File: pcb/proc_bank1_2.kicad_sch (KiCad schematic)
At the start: 1 part

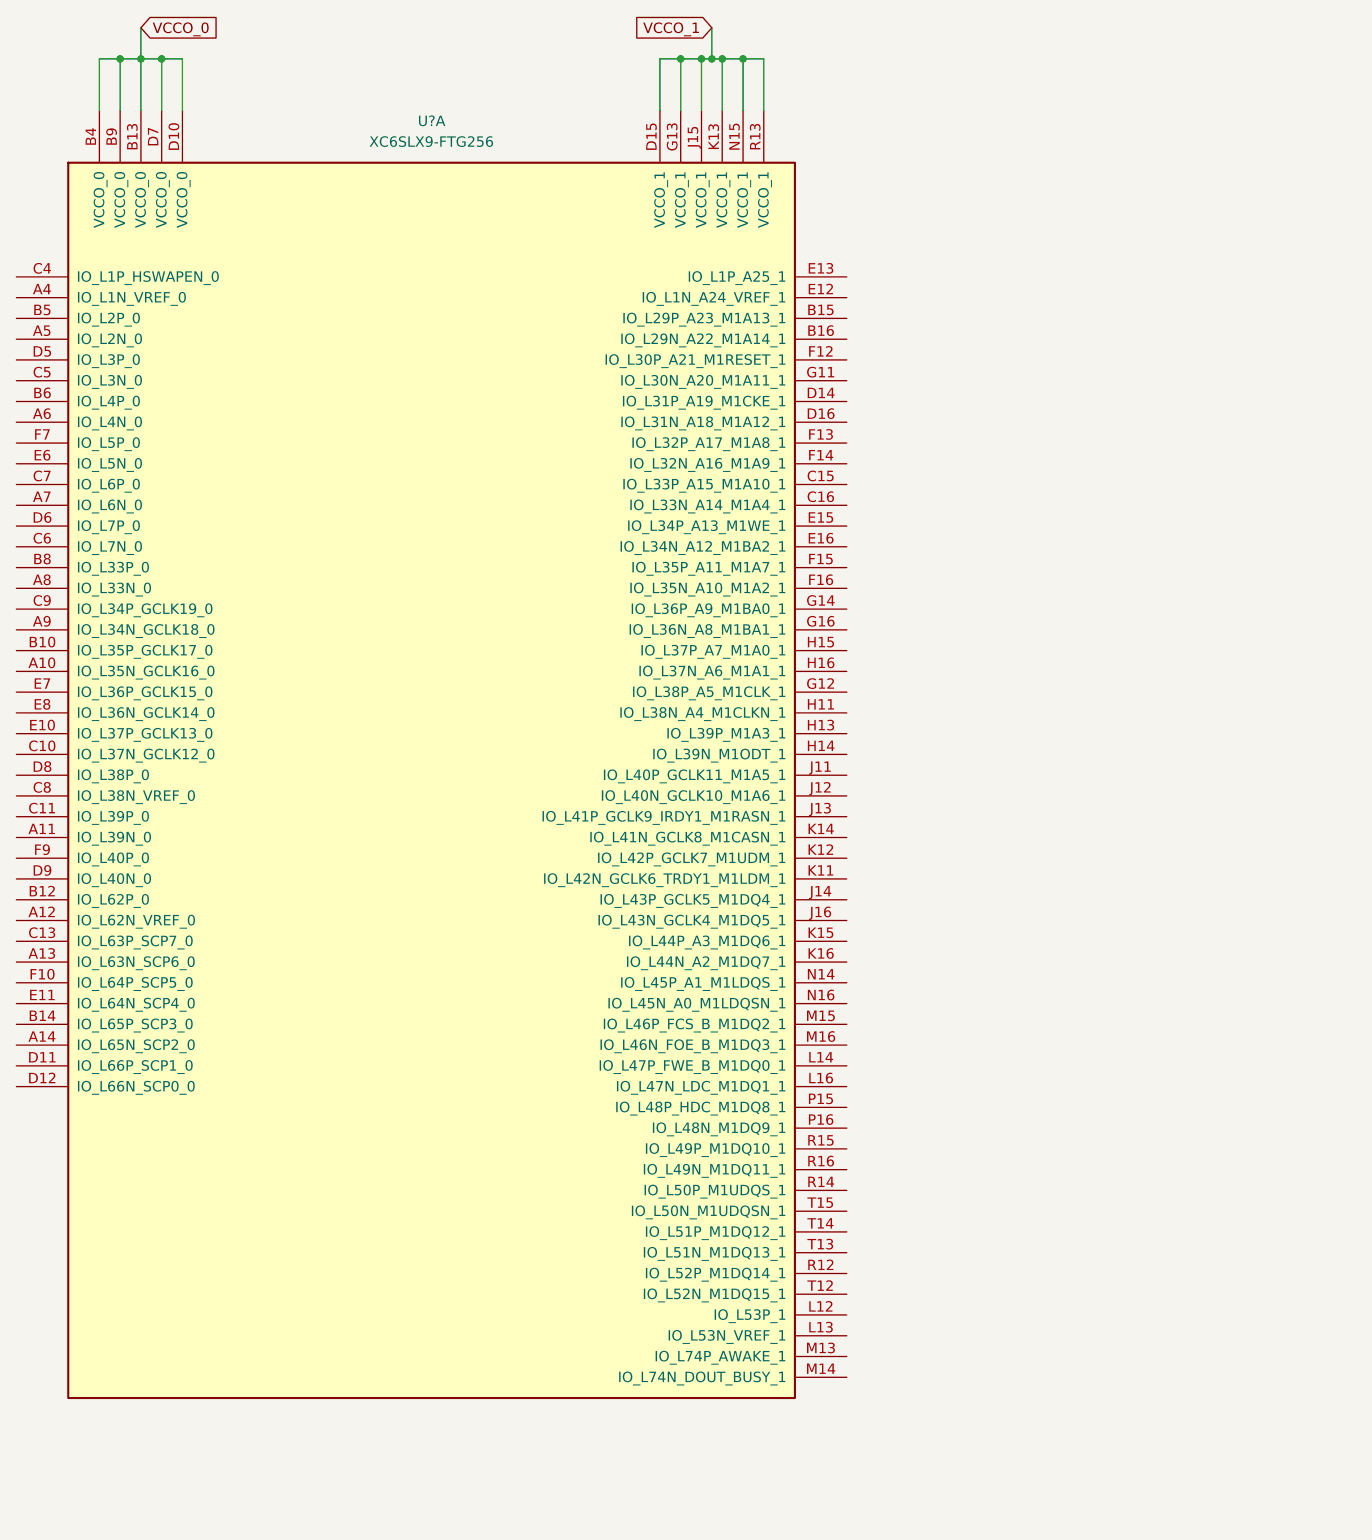
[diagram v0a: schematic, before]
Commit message: add flash memory
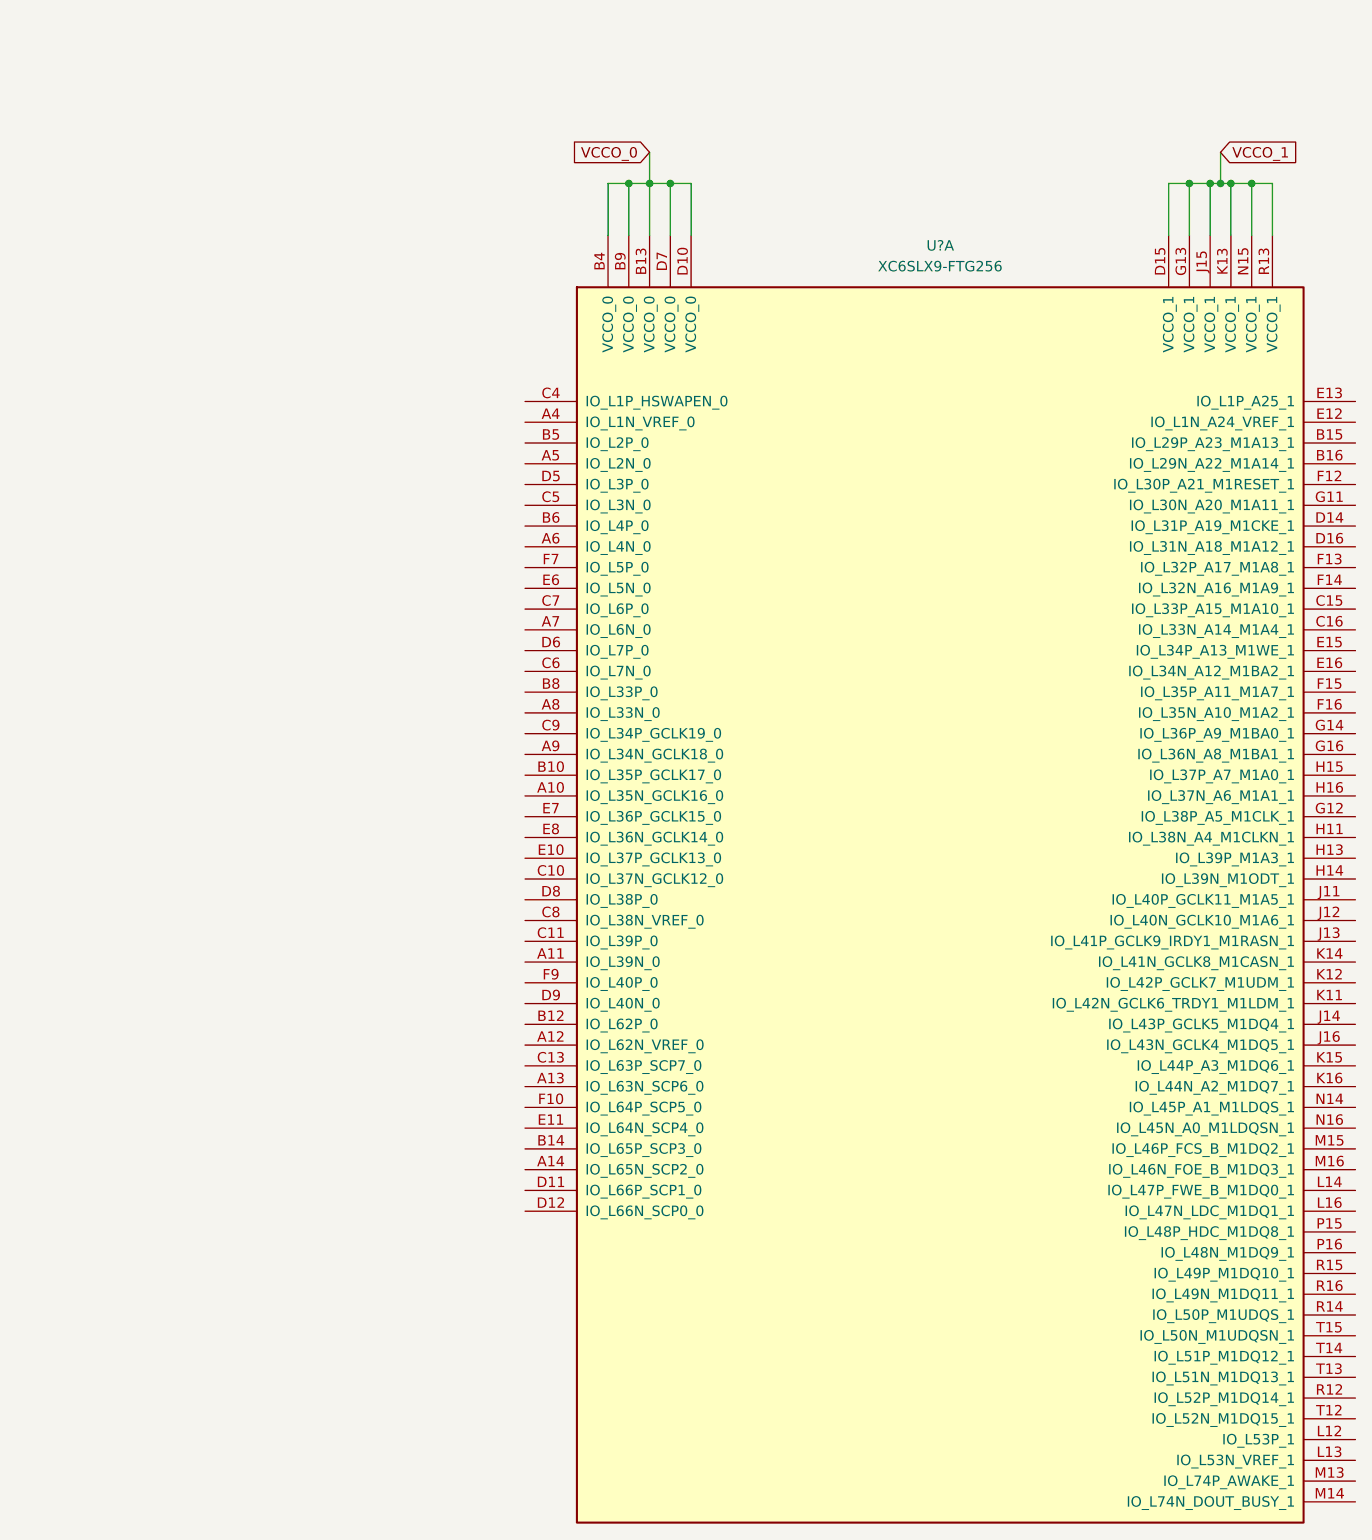
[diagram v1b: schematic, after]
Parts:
- removed U?: XC6SLX9-FTG256, symbol FPGA_Xilinx_Spartan6:XC6SLX9-FTG256
- added U?: XC6SLX9-FTG256, symbol FPGA_Xilinx_Spartan6:XC6SLX9-FTG256
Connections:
- net VCCO_0: now also U?.B13 (VCCO_0), U?.B4 (VCCO_0), U?.B9 (VCCO_0), U?.D10 (VCCO_0), U?.D7 (VCCO_0)
- net VCCO_1: now also U?.D15 (VCCO_1), U?.G13 (VCCO_1), U?.J15 (VCCO_1), U?.K13 (VCCO_1), U?.N15 (VCCO_1), U?.R13 (VCCO_1)
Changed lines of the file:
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@@
 (kicad_sch (version 20210126) (generator eeschema)
-  (paper "User" 200 240.005)
-  (junction (at 60.96 33.02) (diameter 0.9144) (color 0 0 0 0))
-  (junction (at 63.5 33.02) (diameter 0.9144) (color 0 0 0 0))
-  (junction (at 66.04 33.02) (diameter 0.9144) (color 0 0 0 0))
-  (junction (at 129.54 33.02) (diameter 0.9144) (color 0 0 0 0))
-  (junction (at 132.08 33.02) (diameter 0.9144) (color 0 0 0 0))
-  (junction (at 133.35 33.02) (diameter 0.9144) (color 0 0 0 0))
-  (junction (at 134.62 33.02) (diameter 0.9144) (color 0 0 0 0))
-  (junction (at 137.16 33.02) (diameter 0.9144) (color 0 0 0 0))
-  (wire (pts (xy 58.42 33.02) (xy 60.96 33.02))
+  (paper "User" 319.989 280.01)
+  (junction (at 123.19 48.26) (diameter 0.9144) (color 0 0 0 0))
+  (junction (at 125.73 48.26) (diameter 0.9144) (color 0 0 0 0))
+  (junction (at 128.27 48.26) (diameter 0.9144) (color 0 0 0 0))
+  (junction (at 191.77 48.26) (diameter 0.9144) (color 0 0 0 0))
+  (junction (at 194.31 48.26) (diameter 0.9144) (color 0 0 0 0))
+  (junction (at 195.58 48.26) (diameter 0.9144) (color 0 0 0 0))
+  (junction (at 196.85 48.26) (diameter 0.9144) (color 0 0 0 0))
+  (junction (at 199.39 48.26) (diameter 0.9144) (color 0 0 0 0))
+  (wire (pts (xy 120.65 48.26) (xy 123.19 48.26))
     (stroke (width 0) (type solid) (color 0 0 0 0))
   )
-  (wire (pts (xy 58.42 39.37) (xy 58.42 33.02))
+  (wire (pts (xy 120.65 54.61) (xy 120.65 48.26))
     (stroke (width 0) (type solid) (color 0 0 0 0))
   )
-  (wire (pts (xy 60.96 33.02) (xy 60.96 39.37))
+  (wire (pts (xy 123.19 48.26) (xy 123.19 54.61))
     (stroke (width 0) (type solid) (color 0 0 0 0))
   )
-  (wire (pts (xy 60.96 33.02) (xy 63.5 33.02))
+  (wire (pts (xy 123.19 48.26) (xy 125.73 48.26))
     (stroke (width 0) (type solid) (color 0 0 0 0))
   )
-  (wire (pts (xy 63.5 29.21) (xy 63.5 33.02))
+  (wire (pts (xy 125.73 44.45) (xy 125.73 48.26))
     (stroke (width 0) (type solid) (color 0 0 0 0))
   )
-  (wire (pts (xy 63.5 33.02) (xy 63.5 39.37))
+  (wire (pts (xy 125.73 48.26) (xy 125.73 54.61))
     (stroke (width 0) (type solid) (color 0 0 0 0))
   )
-  (wire (pts (xy 66.04 33.02) (xy 63.5 33.02))
+  (wire (pts (xy 128.27 48.26) (xy 125.73 48.26))
     (stroke (width 0) (type solid) (color 0 0 0 0))
   )
-  (wire (pts (xy 66.04 39.37) (xy 66.04 33.02))
+  (wire (pts (xy 128.27 54.61) (xy 128.27 48.26))
     (stroke (width 0) (type solid) (color 0 0 0 0))
   )
-  (wire (pts (xy 68.58 33.02) (xy 66.04 33.02))
+  (wire (pts (xy 130.81 48.26) (xy 128.27 48.26))
     (stroke (width 0) (type solid) (color 0 0 0 0))
   )
-  (wire (pts (xy 68.58 39.37) (xy 68.58 33.02))
+  (wire (pts (xy 130.81 54.61) (xy 130.81 48.26))
     (stroke (width 0) (type solid) (color 0 0 0 0))
   )
-  (wire (pts (xy 127 33.02) (xy 129.54 33.02))
+  (wire (pts (xy 189.23 48.26) (xy 191.77 48.26))
     (stroke (width 0) (type solid) (color 0 0 0 0))
   )
-  (wire (pts (xy 127 39.37) (xy 127 33.02))
+  (wire (pts (xy 189.23 54.61) (xy 189.23 48.26))
     (stroke (width 0) (type solid) (color 0 0 0 0))
   )
-  (wire (pts (xy 129.54 33.02) (xy 129.54 39.37))
+  (wire (pts (xy 191.77 48.26) (xy 194.31 48.26))
     (stroke (width 0) (type solid) (color 0 0 0 0))
   )
-  (wire (pts (xy 129.54 33.02) (xy 132.08 33.02))
+  (wire (pts (xy 191.77 54.61) (xy 191.77 48.26))
     (stroke (width 0) (type solid) (color 0 0 0 0))
   )
-  (wire (pts (xy 132.08 33.02) (xy 132.08 39.37))
+  (wire (pts (xy 194.31 48.26) (xy 194.31 54.61))
     (stroke (width 0) (type solid) (color 0 0 0 0))
   )
-  (wire (pts (xy 132.08 33.02) (xy 133.35 33.02))
+  (wire (pts (xy 194.31 48.26) (xy 195.58 48.26))
     (stroke (width 0) (type solid) (color 0 0 0 0))
   )
-  (wire (pts (xy 133.35 29.21) (xy 133.35 33.02))
+  (wire (pts (xy 195.58 44.45) (xy 195.58 48.26))
     (stroke (width 0) (type solid) (color 0 0 0 0))
   )
-  (wire (pts (xy 134.62 33.02) (xy 133.35 33.02))
+  (wire (pts (xy 195.58 48.26) (xy 196.85 48.26))
     (stroke (width 0) (type solid) (color 0 0 0 0))
   )
-  (wire (pts (xy 134.62 33.02) (xy 137.16 33.02))
+  (wire (pts (xy 196.85 48.26) (xy 196.85 54.61))
     (stroke (width 0) (type solid) (color 0 0 0 0))
   )
-  (wire (pts (xy 134.62 39.37) (xy 134.62 33.02))
+  (wire (pts (xy 199.39 48.26) (xy 196.85 48.26))
     (stroke (width 0) (type solid) (color 0 0 0 0))
   )
-  (wire (pts (xy 137.16 33.02) (xy 139.7 33.02))
+  (wire (pts (xy 199.39 54.61) (xy 199.39 48.26))
     (stroke (width 0) (type solid) (color 0 0 0 0))
   )
-  (wire (pts (xy 137.16 39.37) (xy 137.16 33.02))
+  (wire (pts (xy 201.93 48.26) (xy 199.39 48.26))
     (stroke (width 0) (type solid) (color 0 0 0 0))
   )
-  (wire (pts (xy 139.7 39.37) (xy 139.7 33.02))
+  (wire (pts (xy 201.93 54.61) (xy 201.93 48.26))
     (stroke (width 0) (type solid) (color 0 0 0 0))
   )
-  (global_label "VCCO_0" (shape input) (at 63.5 29.21 0) (fields_autoplaced)
+  (global_label "VCCO_0" (shape input) (at 125.73 44.45 180) (fields_autoplaced)
+    (effects (font (size 1.27 1.27)) (justify right))
+    (property "Intersheet References" "${INTERSHEET_REFS}" (id 0) (at 116.1807 44.3706 0)
+      (effects (font (size 1.27 1.27)) (justify right) hide)
+    )
+  )
+  (global_label "VCCO_1" (shape input) (at 195.58 44.45 0) (fields_autoplaced)
     (effects (font (size 1.27 1.27)) (justify left))
-    (property "Intersheet References" "${INTERSHEET_REFS}" (id 0) (at 73.0493 29.1306 0)
+    (property "Intersheet References" "${INTERSHEET_REFS}" (id 0) (at 205.1293 44.3706 0)
       (effects (font (size 1.27 1.27)) (justify left) hide)
     )
   )
-  (global_label "VCCO_1" (shape input) (at 133.35 29.21 180) (fields_autoplaced)
-    (effects (font (size 1.27 1.27)) (justify right))
-    (property "Intersheet References" "${INTERSHEET_REFS}" (id 0) (at 123.8007 29.2894 0)
-      (effects (font (size 1.27 1.27)) (justify right) hide)
-    )
-  )
-  (symbol (lib_id "FPGA_Xilinx_Spartan6:XC6SLX9-FTG256") (at 99.06 118.11 0) (unit 1)
+  (symbol (lib_id "FPGA_Xilinx_Spartan6:XC6SLX9-FTG256") (at 161.29 133.35 0) (unit 1)
     (in_bom yes) (on_board yes)
-    (property "Reference" "U?" (id 0) (at 99.06 40.64 0))
-    (property "Value" "XC6SLX9-FTG256" (id 1) (at 99.06 43.18 0))
-    (property "Footprint" "" (id 2) (at 99.06 118.11 0)
+    (property "Reference" "U?" (id 0) (at 161.29 55.88 0))
+    (property "Value" "XC6SLX9-FTG256" (id 1) (at 161.29 58.42 0))
+    (property "Footprint" "" (id 2) (at 161.29 133.35 0)
       (effects (font (size 1.27 1.27)) hide)
     )
-    (property "Datasheet" "" (id 3) (at 99.06 118.11 0))
+    (property "Datasheet" "" (id 3) (at 161.29 133.35 0))
     (pin "A10")
     (pin "A11")
